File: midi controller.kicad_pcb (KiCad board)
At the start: 2 copper layers, 260 x 140 mm, 59 parts, among them J1 Conn_01x04, SW1 SW_Push, SW2 SW_Push, SW3 SW_Push, SW4 SW_Push, U1 Teensy4.0-d

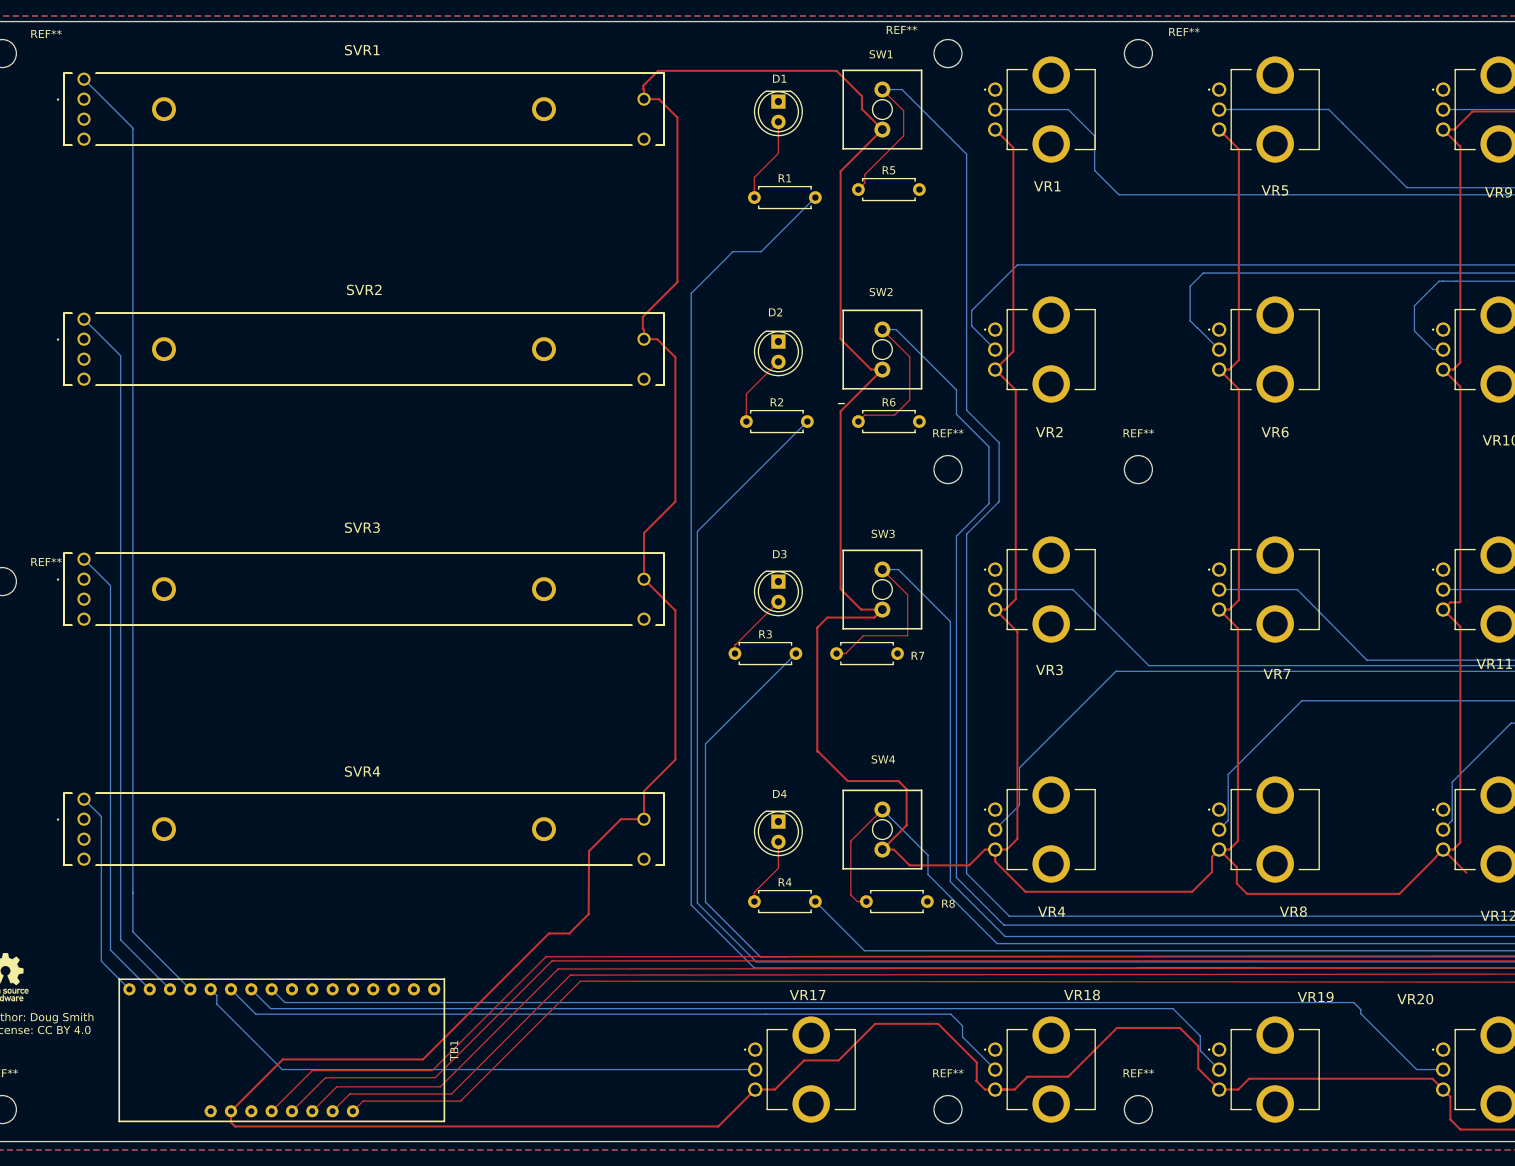
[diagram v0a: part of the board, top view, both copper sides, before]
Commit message: updated the fader and switch devices
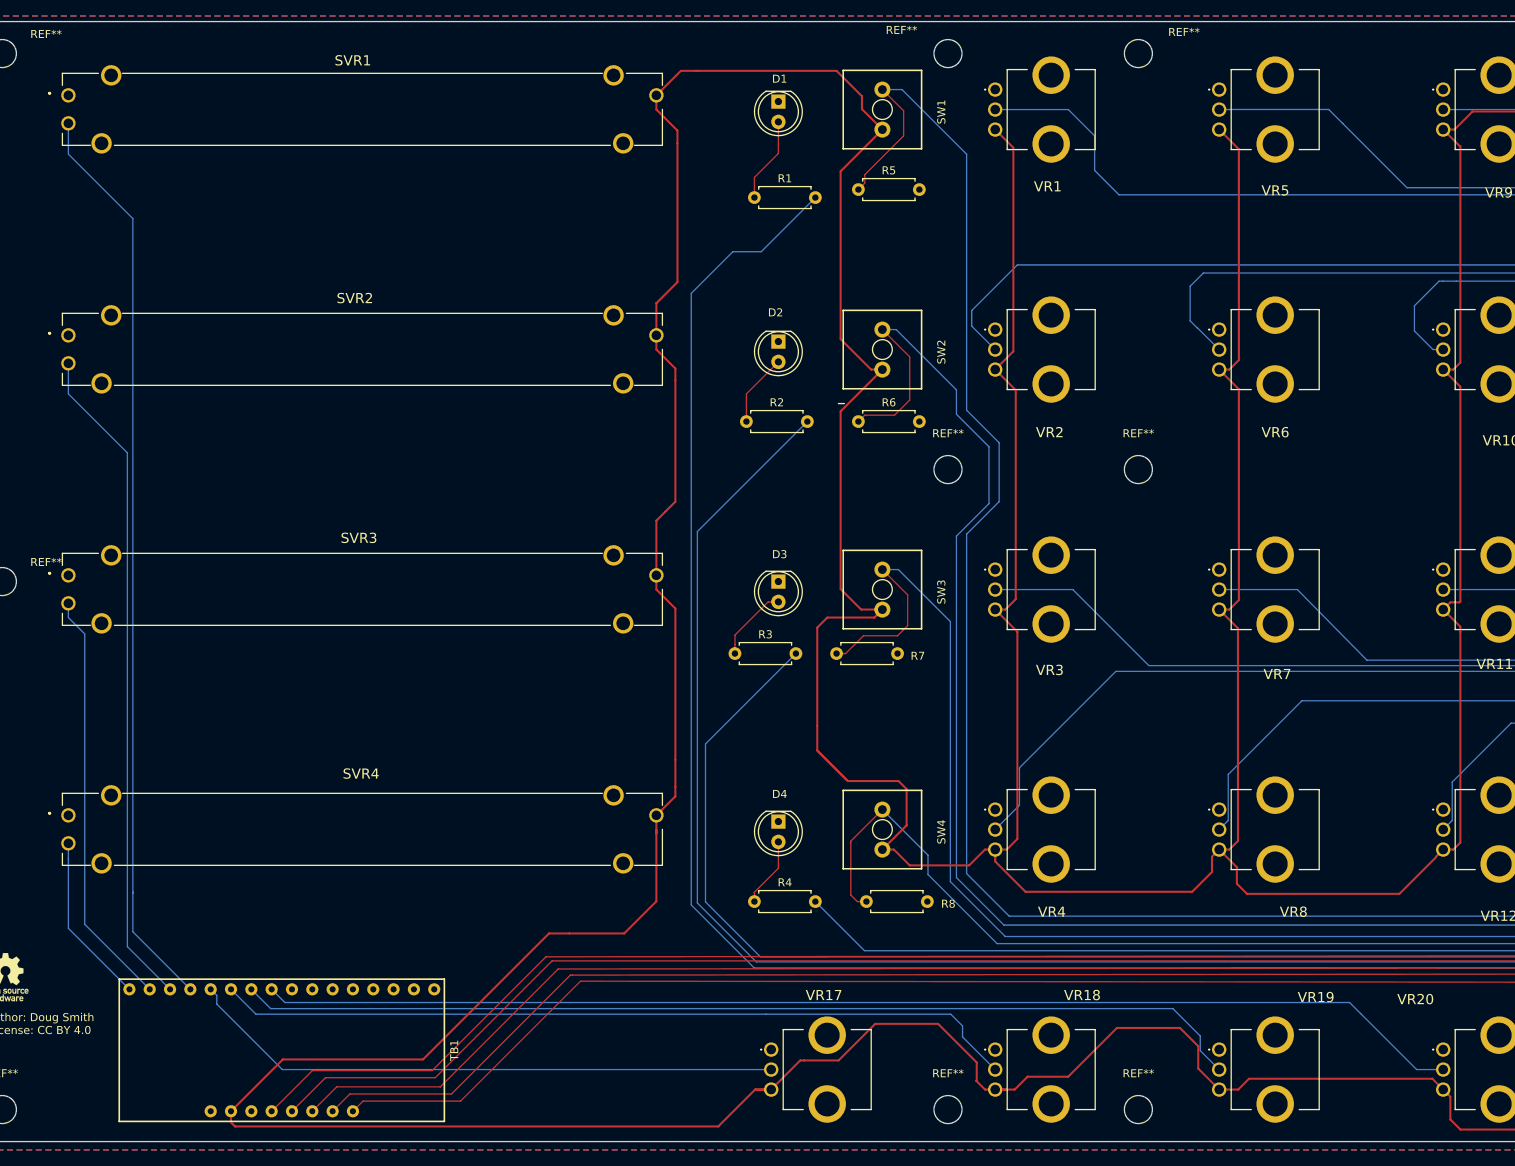
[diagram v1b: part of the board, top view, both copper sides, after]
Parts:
- SVR1, SVR2, SVR3, SVR4: value RS6011SP6003 -> PTA6043-2015CPB103; footprint SamacSys_Parts:RS6011SP6003 -> PTA6043-2015CPB103:PTA60432015CPB103
- SW1, SW2, SW3, SW4: footprint midi controller:1543-650-149 -> midi controller:800SP9B7M2QE
- moved VR17 2.00 mm to (127.0, 151.0)
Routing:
- net /SL3: track 57.2 -> 52.5 mm
- net /SL2: track 88.2 -> 83.5 mm
- net /SL1: track 119.5 -> 114.7 mm
- net /SL4: track 26.1 -> 21.6 mm
- net /PT17: track 72.8 -> 74.8 mm
- net 3V3: track 1098.3 -> 1097.1 mm
- net /SW2: track 180.4 -> 179.6 mm
- net Net-(D3-Pad2): track 8.77 -> 9.45 mm
